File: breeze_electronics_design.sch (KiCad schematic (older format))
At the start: 100 parts, among them U1 STM32F103T8U6TR

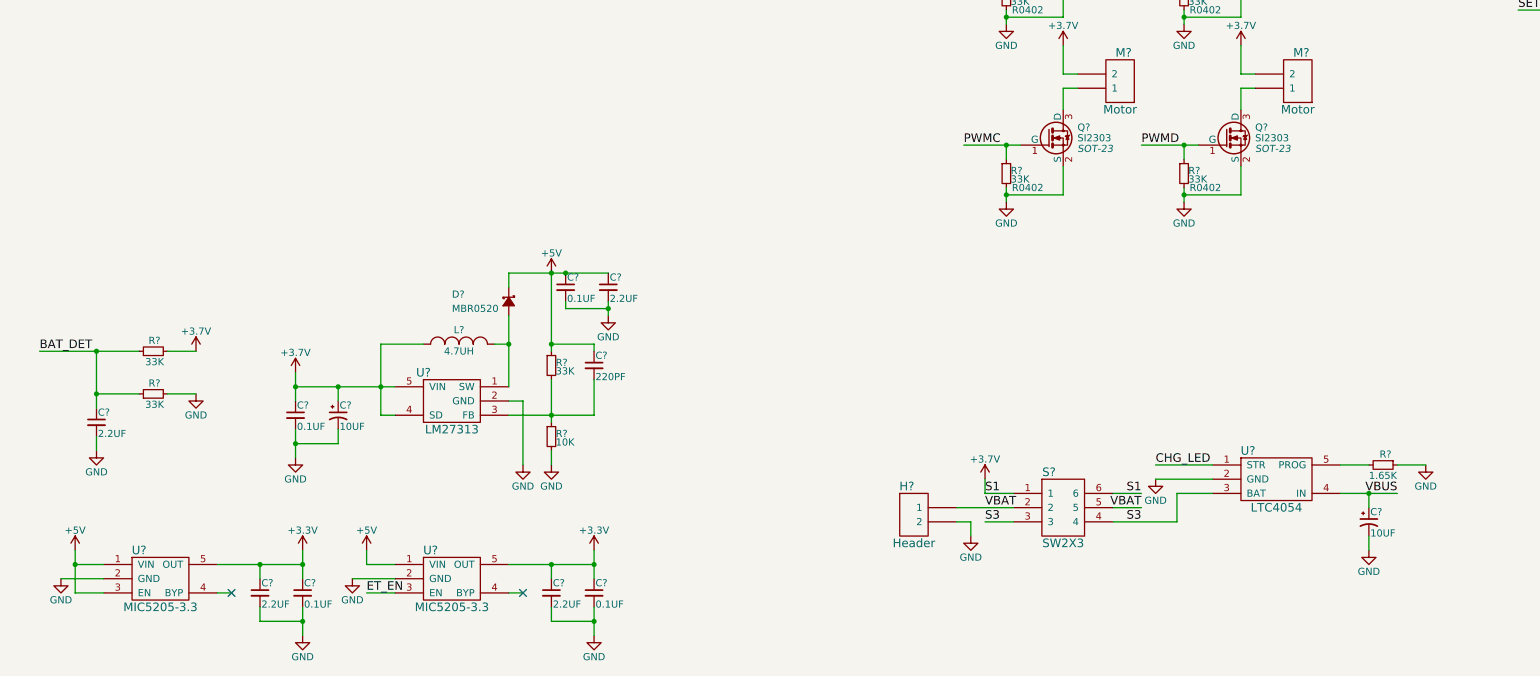
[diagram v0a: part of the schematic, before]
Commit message: Modify the schematic of power
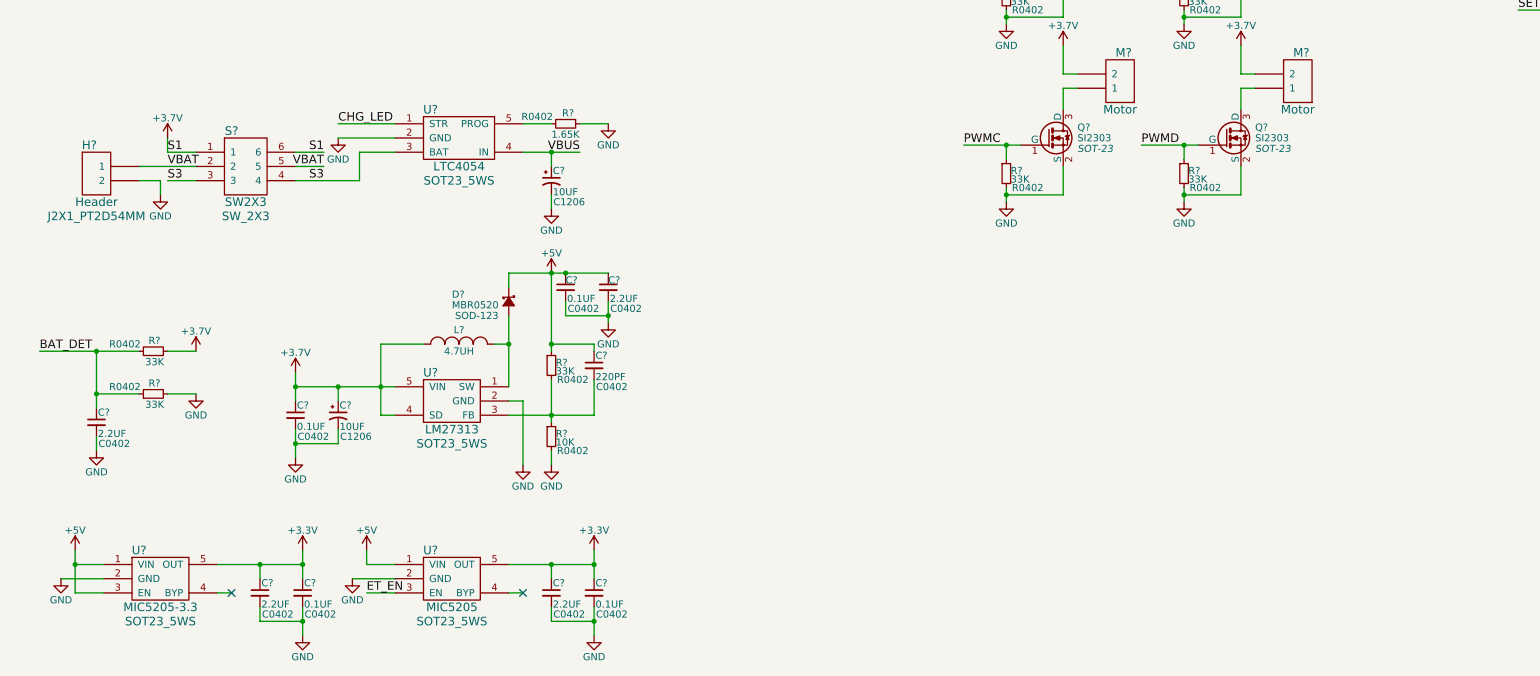
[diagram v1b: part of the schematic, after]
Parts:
- removed U?: MIC5205-3.3, symbol MIC5205-3.3
- added U?: MIC5205, SOT23_5WS, symbol MIC5205
- C? (x9): footprint (none) -> C0402
- C?: footprint (none) -> C1206
- D?: footprint (none) -> SOD-123
- H?: footprint (none) -> J2X1_PT2D54MM
- R? (x5): footprint (none) -> R0402
- S?: footprint (none) -> SW_2X3
- U? (x3): footprint (none) -> SOT23_5WS
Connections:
- net ET_EN: now also U?.3 (EN)
- net at C?.1, C?.1: now also U?.5 (OUT)
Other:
- moved on the sheet: C?, H?, R?, S?, U?

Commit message: Fix some ERC's errors
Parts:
- L1: renamed from L?; footprint (none) -> L0402
- gave numbers to parts that had none: 98
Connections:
- net ET_EN is gone; now on net BT_EN: U5.3 (EN)
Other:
- moved on the sheet: C6, D1, Q1, R7, U3, USB1

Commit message: Add voltage and accuracy fields
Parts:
- C1, C10, C12, C13, C14, C21, C24, C27, C30, C7, C8: Voltage (none) -> 16V
- C11, C15, C16, C2, C25, C26, C29, C3, C31, C32, C33, C4, C5, C6: Voltage (none) -> 10V
- C28: Voltage (none) -> 6.3V
- C9: footprint (none) -> C1206; Voltage (none) -> 16V
- R1, R2, R20, R21, R22, R23, R3, R5, R8: Accuracy (none) -> 1%
- R10, R11, R12, R13, R14, R15, R16, R17, R18, R19, R4, R6, R7, R9: Accuracy (none) -> 5%
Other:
- note removed: "Controller"
- moved on the sheet: D1, D3, J1, LED1, LED10, LED2, LED3, LED4, LED5, LED6, LED7, LED8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

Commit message: Modify the format of components
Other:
- moved on the sheet: A1, C19, C22, C23, C24, C26, C33, L2, L3, L4, U9

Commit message: Finish the schematic
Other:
- note added: "LEDs"
- note added: "MCU\n"
- note added: "Motors"
- note added: "Power"
- note added: "Sensors"
- note added: "Serial"
- note added: "Wireless"
- moved on the sheet: A1, C1, C10, C11, C12, C13, C14, C15, C16, C17, C18, C19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

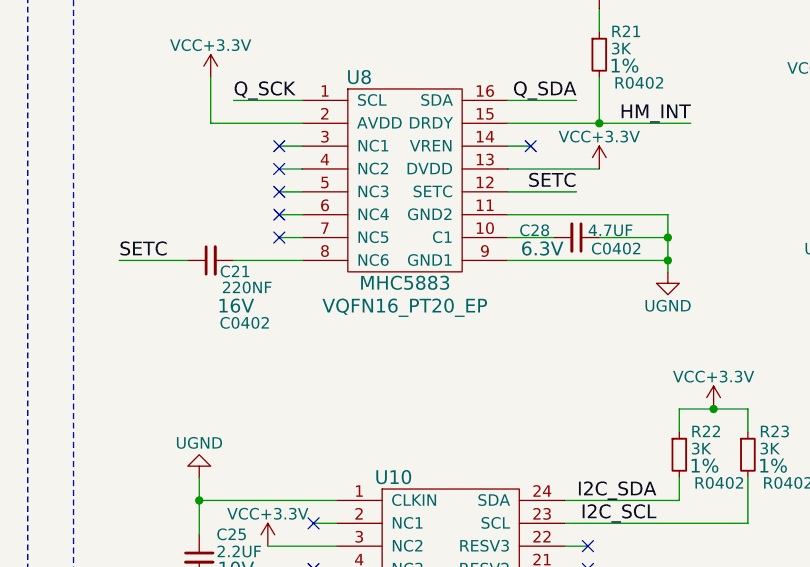
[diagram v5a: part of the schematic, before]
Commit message: Fix HMC5883L's name
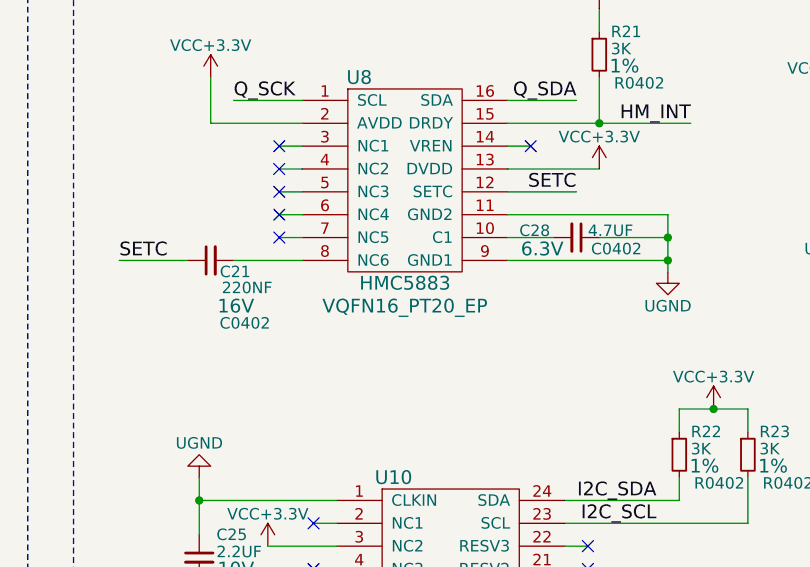
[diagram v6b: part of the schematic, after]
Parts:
- U8: value MHC5883 -> HMC5883
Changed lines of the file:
@@
 P 7450 7550
 F 0 "U8" H 7250 8000 60  0000 C CNN
-F 1 "MHC5883" H 7450 7100 60  0000 C CNN
+F 1 "HMC5883" H 7450 7100 60  0000 C CNN
 F 2 "VQFN16_PT20_EP" H 7450 7000 60  0000 C CNN
 F 3 "" H 7400 7750 60  0000 C CNN

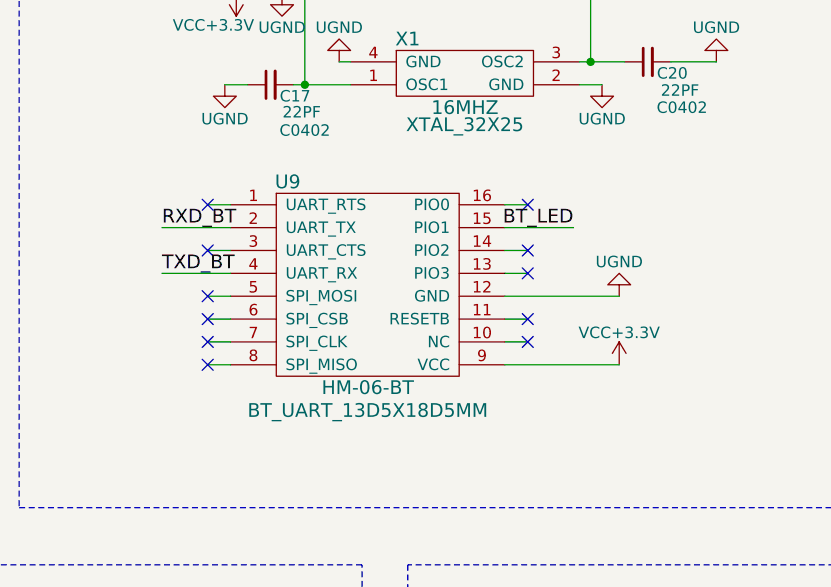
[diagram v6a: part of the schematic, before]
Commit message: Modify the HM-06-BT
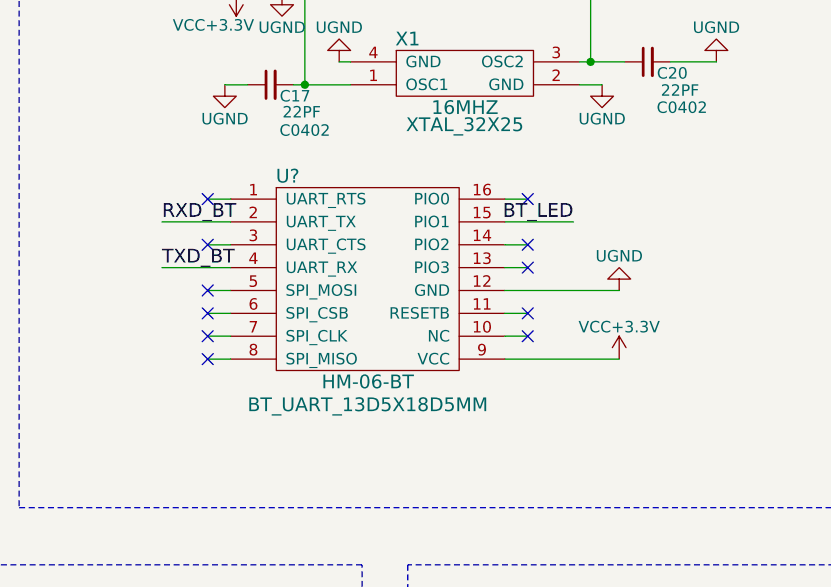
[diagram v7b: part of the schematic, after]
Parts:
- removed U9: HM-06-BT, BT_UART_13D5X18D5MM, symbol HM-06-BT
- added U?: HM-06-BT, BT_UART_13D5X18D5MM, symbol HM-06-BT
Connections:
- net BT_LED: now also U?.15 (PIO1)
- net RXD_BT: now also U?.2 (UART_TX)
- net TXD_BT: now also U?.4 (UART_RX)
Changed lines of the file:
@@
 EESchema Schematic File Version 2
+LIBS:breeze_electronics_design-rescue
 LIBS:power
 LIBS:device
@@
 	1    0    0    -1
 $EndComp
-$Comp
-L HM-06-BT U9
-U 1 1 57B51355
-P 11725 5025
-F 0 "U9" H 11375 5425 60  0000 C CNN
-F 1 "HM-06-BT" H 11725 4525 60  0000 C CNN
-F 2 "BT_UART_13D5X18D5MM" H 11725 4425 60  0000 C CNN
-F 3 "" H 11725 5075 60  0000 C CNN
-	1    11725 5025
-	1    0    0    -1
-$EndComp
-NoConn ~ 11025 4725
-NoConn ~ 11025 4925
-NoConn ~ 11025 5125
-NoConn ~ 11025 5225
-NoConn ~ 11025 5325
-NoConn ~ 11025 5425
-NoConn ~ 12425 5325
-NoConn ~ 12425 5225
-NoConn ~ 12425 5025
-NoConn ~ 12425 4725
-NoConn ~ 12425 4925
-Text Label 10825 4825 0    60   ~ 0
+NoConn ~ 11025 4700
+NoConn ~ 11025 4900
+NoConn ~ 11025 5100
+NoConn ~ 11025 5200
+NoConn ~ 11025 5300
+NoConn ~ 11025 5400
+NoConn ~ 12425 5300
+NoConn ~ 12425 5200
+NoConn ~ 12425 5000
+NoConn ~ 12425 4700
+NoConn ~ 12425 4900
+Text Label 10825 4800 0    60   ~ 0
 RXD_BT
-Text Label 10825 5025 0    60   ~ 0
+Text Label 10825 5000 0    60   ~ 0
 TXD_BT
-Text Label 12625 4825 2    60   ~ 0
+Text Label 12625 4800 2    60   ~ 0
 BT_LED
 $Comp
@@
 L VCC+3.3V #PWR04
 U 1 1 57B606EB
-P 12825 5425
-F 0 "#PWR04" H 12825 5275 50  0001 C CNN
-F 1 "VCC+3.3V" H 12825 5565 50  0000 C CNN
-F 2 "" H 12825 5425 50  0000 C CNN
-F 3 "" H 12825 5425 50  0000 C CNN
-	1    12825 5425
+P 12825 5400
+F 0 "#PWR04" H 12825 5250 50  0001 C CNN
+F 1 "VCC+3.3V" H 12825 5540 50  0000 C CNN
+F 2 "" H 12825 5400 50  0000 C CNN
+F 3 "" H 12825 5400 50  0000 C CNN
+	1    12825 5400
 	1    0    0    -1
 $EndComp
@@
 L UGND #PWR057
 U 1 1 57B84F41
-P 12825 5125
-F 0 "#PWR057" H 12825 4875 50  0001 C CNN
-F 1 "UGND" H 12825 4975 50  0000 C CNN
-F 2 "" H 12825 5125 50  0000 C CNN
-F 3 "" H 12825 5125 50  0000 C CNN
-	1    12825 5125
+P 12825 5100
+F 0 "#PWR057" H 12825 4850 50  0001 C CNN
+F 1 "UGND" H 12825 4950 50  0000 C CNN
+F 2 "" H 12825 5100 50  0000 C CNN
+F 3 "" H 12825 5100 50  0000 C CNN
+	1    12825 5100
 	-1   0    0    1
 $EndComp
@@
 	950  1050 950  1000
 Wire Wire Line
-	10825 4825 11125 4825
+	10825 4800 11125 4800
 Wire Wire Line
-	10825 5025 11125 5025
+	10825 5000 11125 5000
 Wire Wire Line
-	11025 4725 11125 4725
+	11025 4700 11125 4700
 Wire Wire Line
-	11025 4925 11125 4925
+	11025 4900 11125 4900
 Wire Wire Line
-	11025 5125 11125 5125
+	11025 5100 11125 5100
 Wire Wire Line
-	11025 5225 11125 5225
+	11025 5200 11125 5200
 Wire Wire Line
-	11025 5325 11125 5325
+	11025 5300 11125 5300
 Wire Wire Line
-	11025 5425 11125 5425
+	11025 5400 11125 5400
 Wire Wire Line
-	12425 4725 12325 4725
+	12425 4700 12325 4700
 Wire Wire Line
-	12425 4925 12325 4925
+	12425 4900 12325 4900
 Wire Wire Line
-	12425 5025 12325 5025
+	12425 5000 12325 5000
 Wire Wire Line
-	12425 5225 12325 5225
+	12425 5200 12325 5200
 Wire Wire Line
-	12425 5325 12325 5325
+	12425 5300 12325 5300
 Wire Wire Line
-	12625 4825 12325 4825
+	12625 4800 12325 4800
 Wire Wire Line
-	12325 5125 12825 5125
+	12325 5100 12825 5100
 Wire Wire Line
-	12825 5425 12325 5425
+	12825 5400 12325 5400
 Wire Wire Line
 	13150 6950 13150 7150
@@
 Wire Notes Line
 	15950 9850 15950 6300
+$Comp
+L HM-06-BT U?
+U 1 1 57B99EFF
+P 11725 5000
+F 0 "U?" H 11375 5400 60  0000 C CNN
+F 1 "HM-06-BT" H 11725 4500 60  0000 C CNN
+F 2 "BT_UART_13D5X18D5MM" H 11725 4400 60  0000 C CNN
+F 3 "" H 11725 5050 60  0000 C CNN
+	1    11725 5000
+	1    0    0    -1
+$EndComp
 $EndSCHEMATC

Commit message: Modify the power's name
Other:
- moved on the sheet: U?, Y1
